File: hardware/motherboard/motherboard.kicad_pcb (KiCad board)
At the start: 2 copper layers, 220 x 150 mm, 28 parts, among them J1 01x02_Screw_ECG, J2 01x02_Screw_5VDC_IN, J3 RCA_L_Female_Tweeter, J4 RCA_R_Female_Sub, U1 DSP-MODULE_IDC_J3, U2 MCU-MODULE, U3 ECG-MODULE, U4 DSP-MODULE_IDC_J4, U5 PROTO-MODULE, U6 DSP-MODULE_JST_J3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

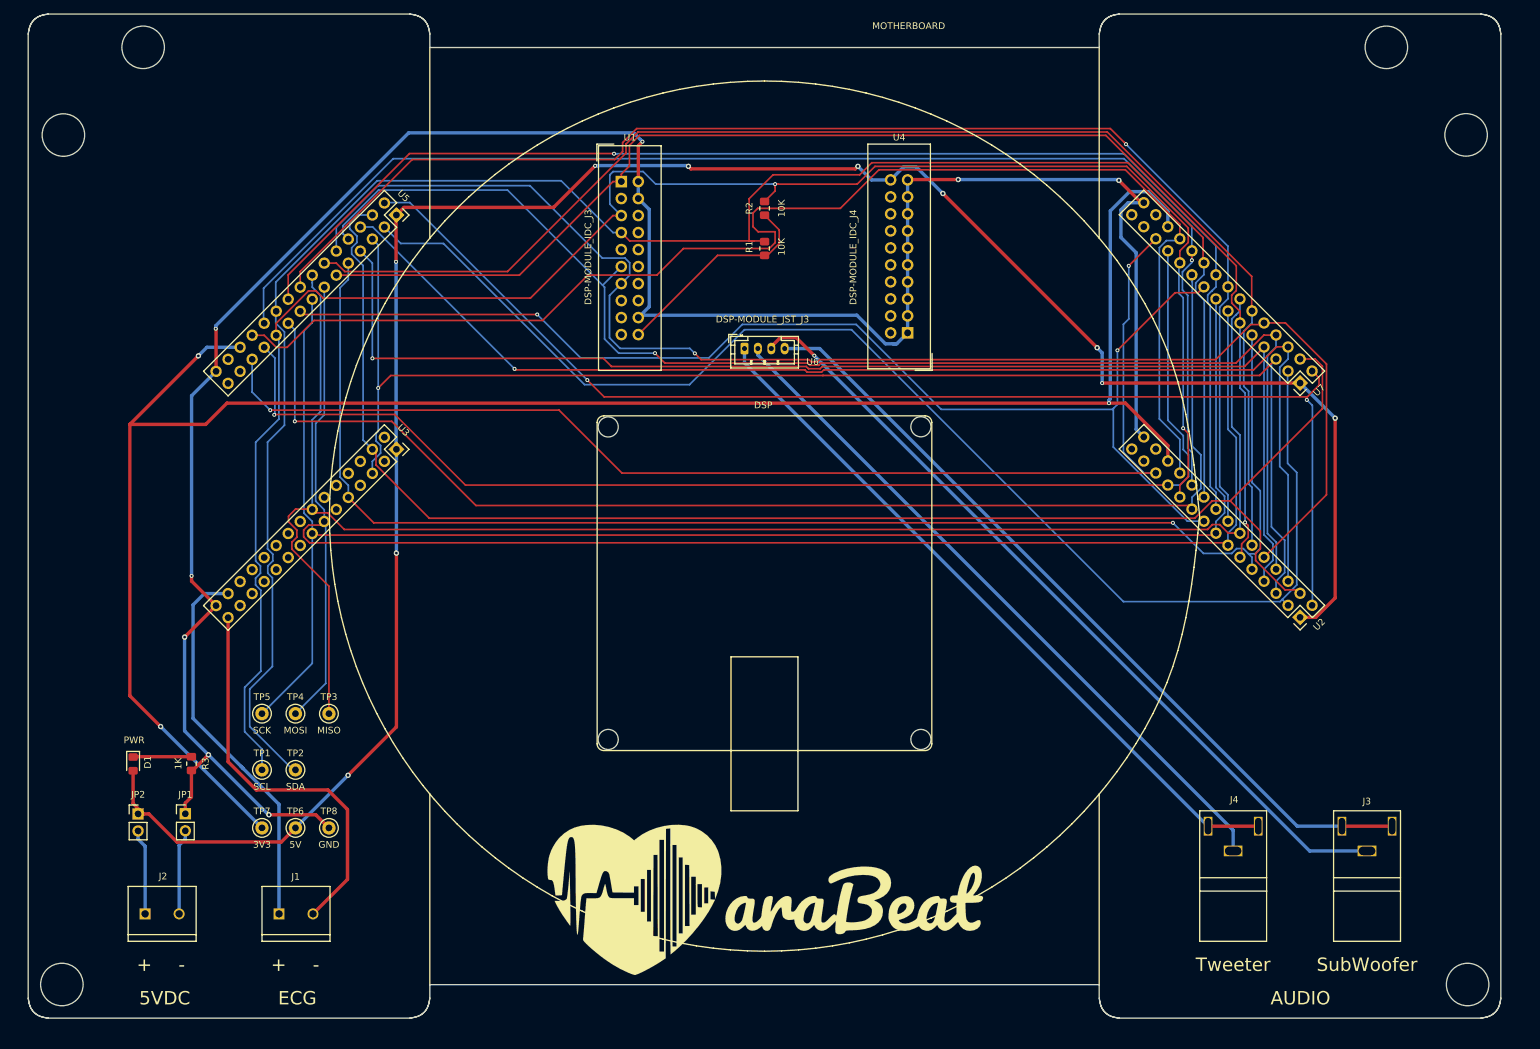
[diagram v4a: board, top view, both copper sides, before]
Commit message: [hw] Add copper pour on both planes
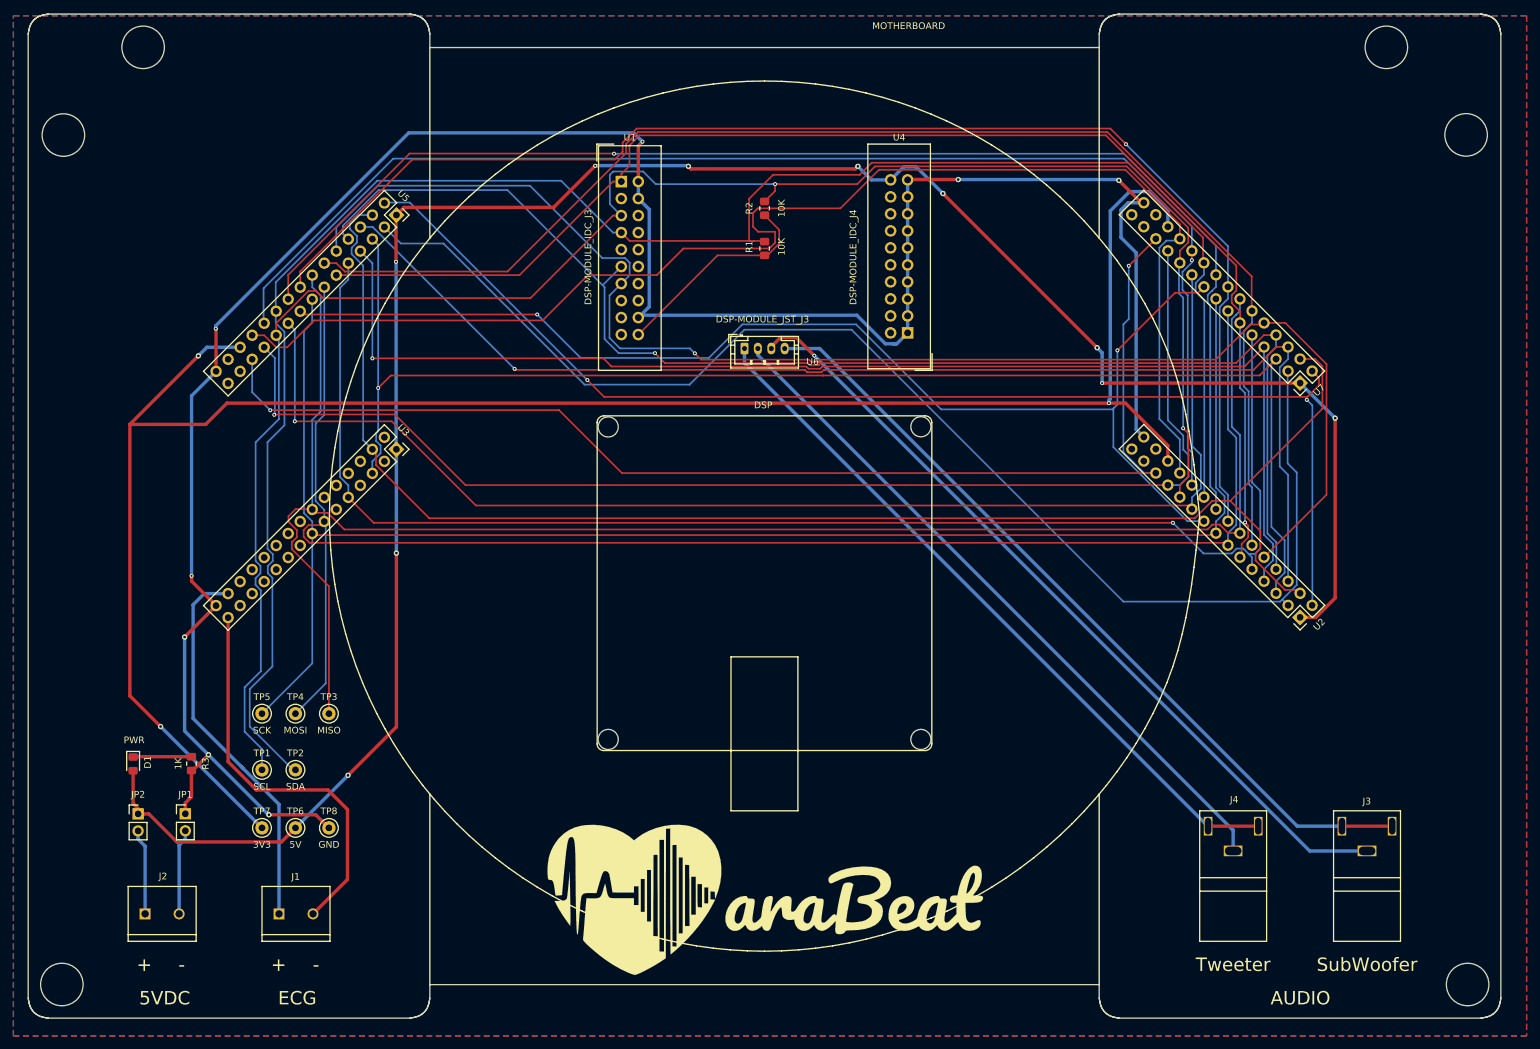
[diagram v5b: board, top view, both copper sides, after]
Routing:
- added copper zone on F.Cu, net 5V
- added copper zone on B.Cu, net GND
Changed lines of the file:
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@@
     (solder_mask_min_width 0.25)
     (aux_axis_origin 129.9845 89.9795)
-    (visible_elements FFFFEF7F)
+    (visible_elements FFFFFF7F)
     (pcbplotparams
       (layerselection 0x010fc_ffffffff)
@@
   (segment (start 43.4665 138.2263) (end 42.54 139.1528) (width 0.508) (layer B.Cu) (net 37))
   (segment (start 42.54 139.1528) (end 42.54 149.4) (width 0.508) (layer B.Cu) (net 37) (status 20))
+  (zone (net 2) (net_name 5V) (layer F.Cu) (hatch edge 0.508)
+    (connect_pads (clearance 0.508))
+    (min_thickness 0.254)
+    (fill yes (arc_segments 16) (thermal_gap 0.508) (thermal_bridge_width 0.508))
+    (polygon
+      (pts
+        (xy 17.78 167.64) (xy 17.78 15.24) (xy 243.84 15.24) (xy 243.84 167.64)
+      )
+    )
+  )
+  (zone (net 1) (net_name GND) (layer B.Cu) (hatch edge 0.508)
+    (connect_pads (clearance 0.508))
+    (min_thickness 0.254)
+    (fill yes (arc_segments 16) (thermal_gap 0.508) (thermal_bridge_width 0.508))
+    (polygon
+      (pts
+        (xy 243.84 167.64) (xy 17.78 167.64) (xy 17.78 15.24) (xy 243.84 15.24)
+      )
+    )
+  )
 )

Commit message: [hw] Add all silkscreen texts to motherboard
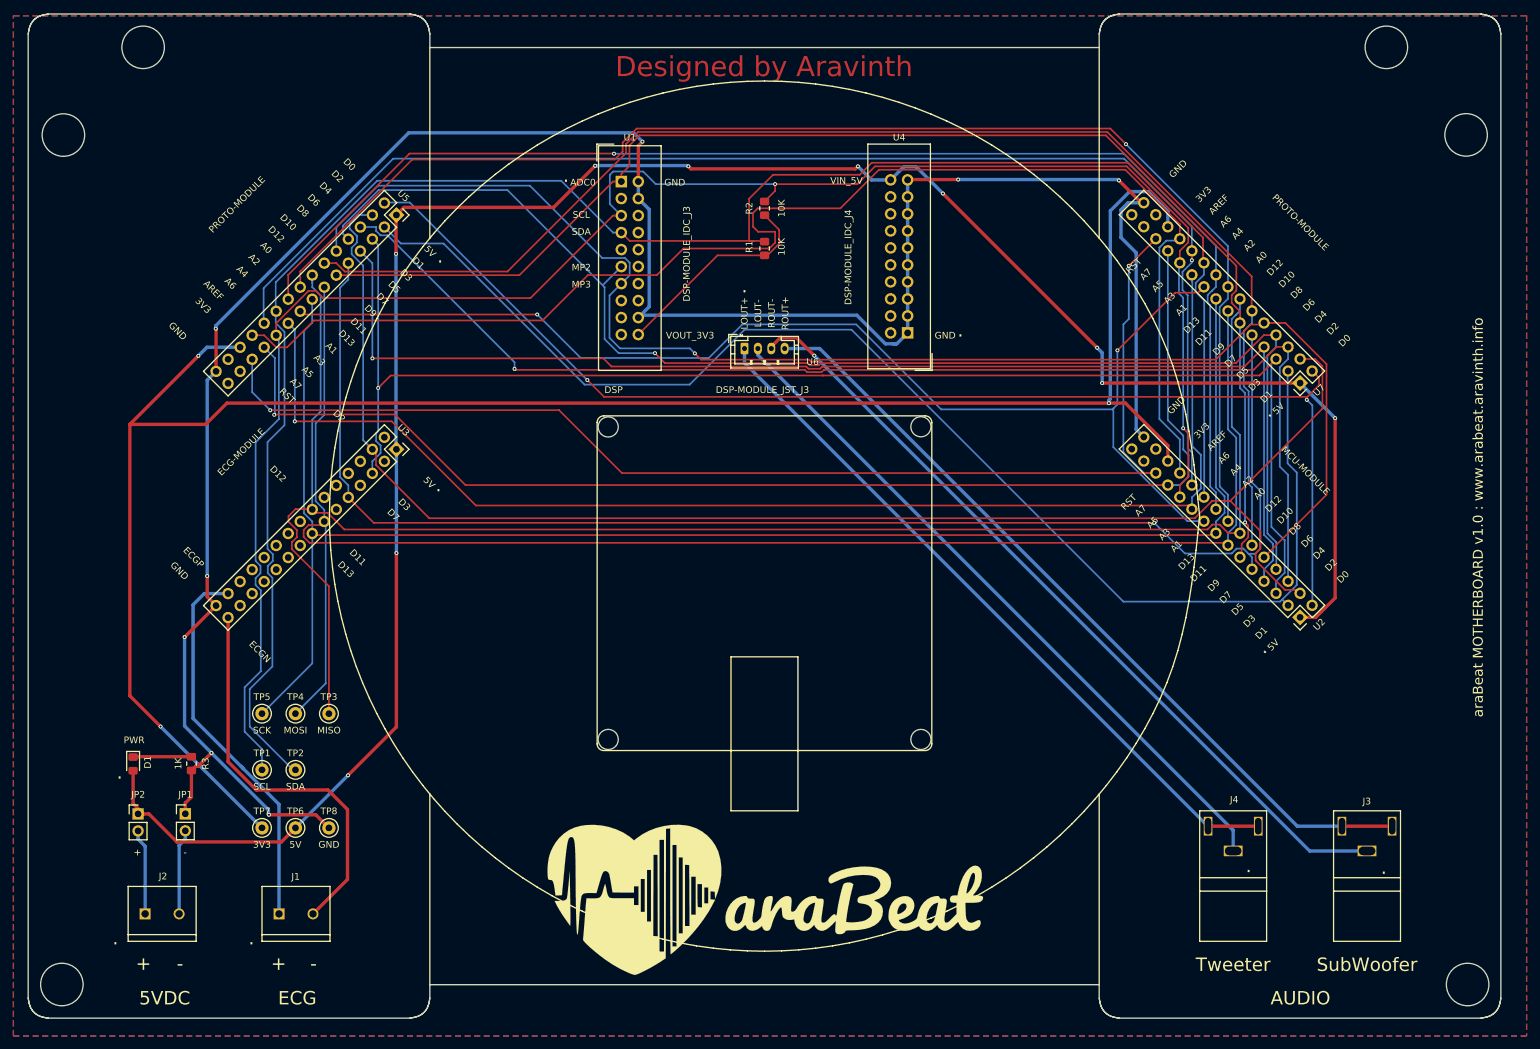
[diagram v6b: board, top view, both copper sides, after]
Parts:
- added G***: LOGO, ARABEAT:MOTHERBOARD-LOGO, B.Cu at (130.0, 95.0)
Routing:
- net GND: track 349.7 -> 348.3 mm
- net D4: track 185.2 -> 186.1 mm
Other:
- board text added: "."
- board text added: "3V3"
- board text added: "5V"
- board text added: "A0"
- board text added: "A1"
- board text added: "A2"
- board text added: "A3"
- board text added: "A4"
- board text added: "A5"
- board text added: "A6"
- board text added: "A7"
- board text added: "ADC0"
- board text added: "AREF"
- board text added: "D0"
- board text added: "D1"
- board text added: "D10"
- board text added: "D11"
- board text added: "D12"
- board text added: "D13"
- board text added: "D2"
- board text added: "D3"
- board text added: "D4"
- board text added: "D5"
- board text added: "D6"
- board text added: "D7"
- board text added: "D8"
- board text added: "D9"
- board text added: "Designed by Aravinth"
- board text added: "ECGN"
- board text added: "ECGP"
- board text added: "GND"
- board text added: "LOUT+"
- board text added: "LOUT-"
- board text added: "MP2"
- board text added: "MP3"
- board text added: "ROUT+"
- board text added: "ROUT-"
- board text added: "RST"
- board text added: "SCL"
- board text added: "SDA"
- board text added: "VIN_5V"
- board text added: "VOUT_3V3"
- board text added: "araBeat MOTHERBOARD v1.0 : Designed by Aravinth www.arabeat.aravinth.info"
- board text added: "araBeat MOTHERBOARD v1.0 : www.arabeat.aravinth.info"
